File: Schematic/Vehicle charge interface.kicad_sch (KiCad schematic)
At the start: 20 parts

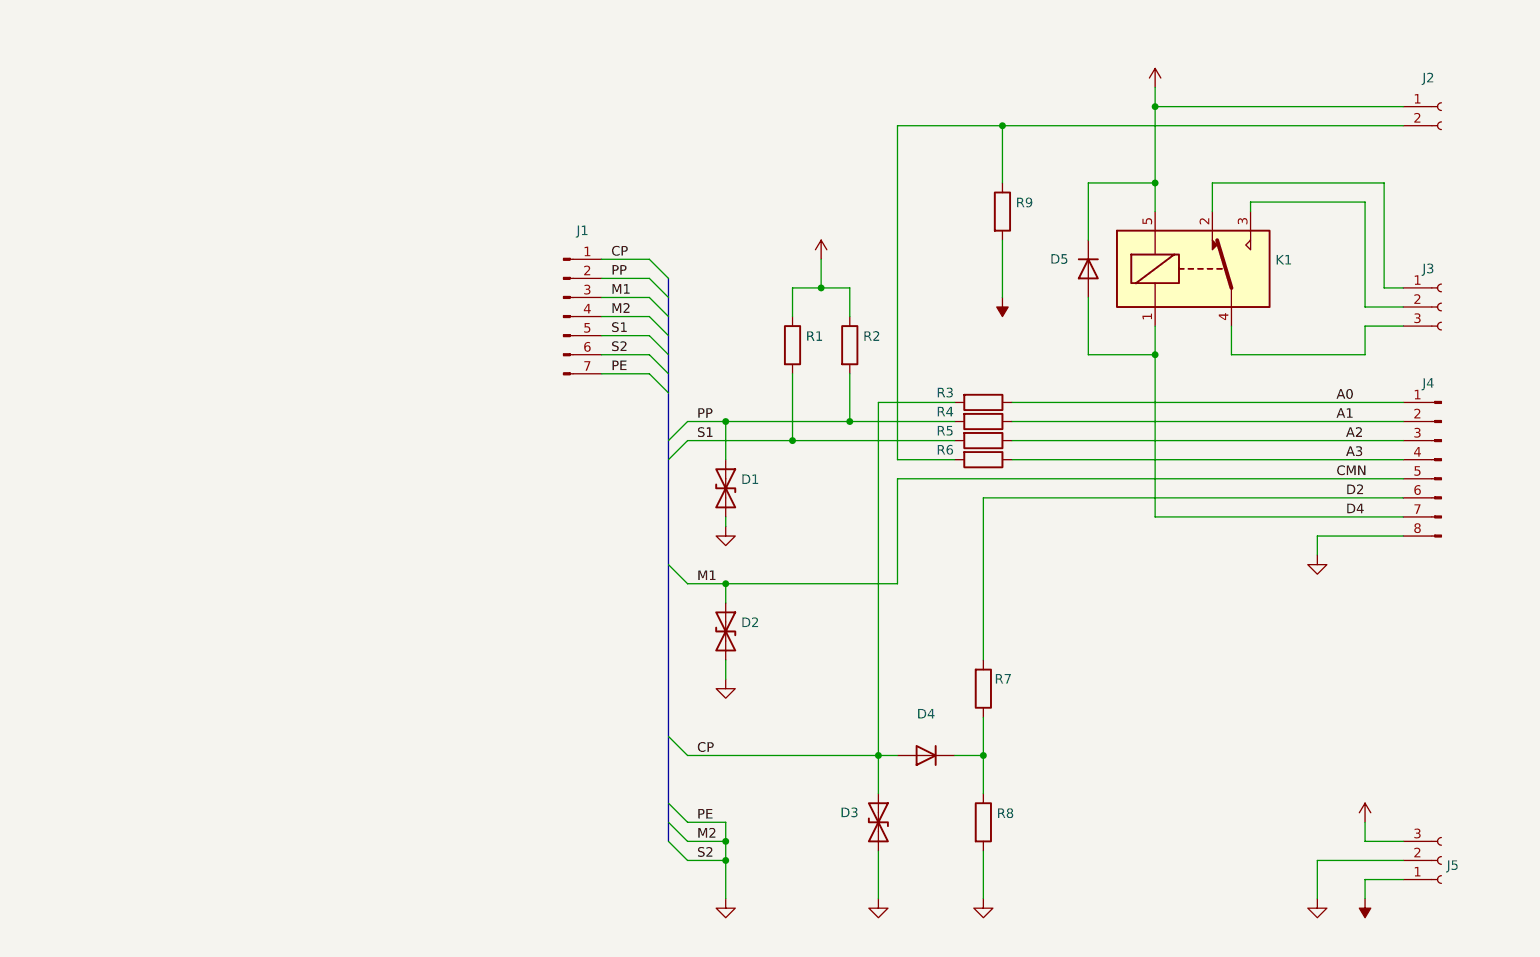
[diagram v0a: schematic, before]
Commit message: Added separate wiring diagram
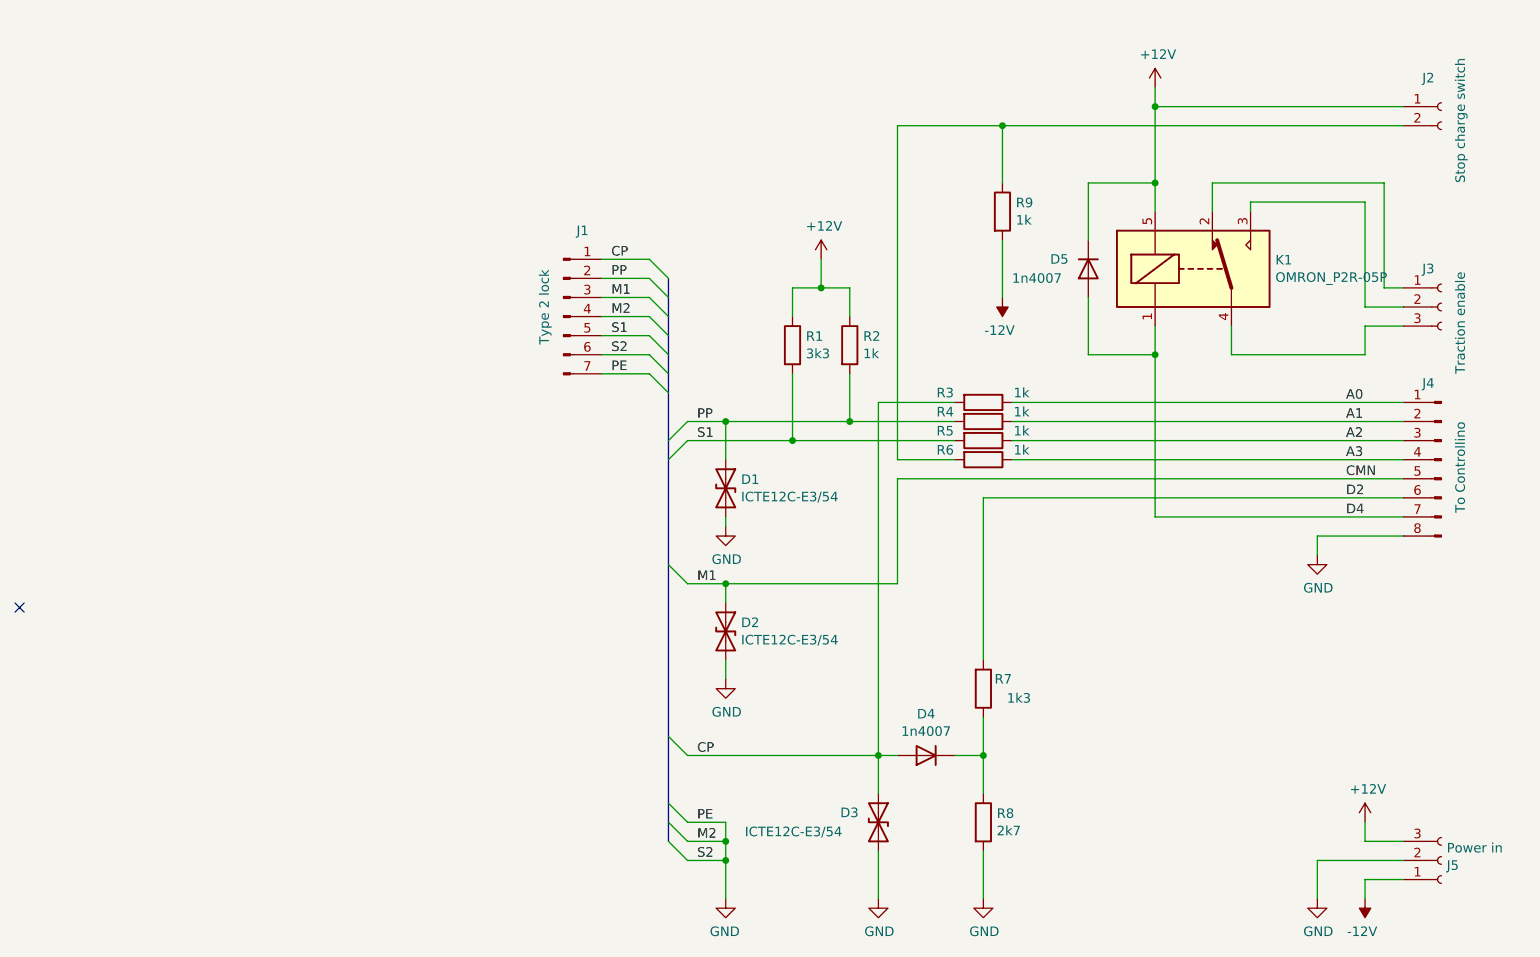
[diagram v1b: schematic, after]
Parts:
- D1, D2, D3: value (none) -> ICTE12C-E3/54; footprint (none) -> Diode_THT:D_DO-201_P15.24mm_Horizontal
- D4, D5: value (none) -> 1n4007; footprint (none) -> Diode_THT:D_DO-41_SOD81_P10.16mm_Horizontal
- J1: value (none) -> Type 2 lock; footprint (none) -> Connector_Wago:Wago_734-137_1x07_P3.50mm_Vertical
- J2: value (none) -> Stop charge switch; footprint (none) -> Connector_Wago:Wago_734-132_1x02_P3.50mm_Vertical
- J3: value (none) -> Traction enable; footprint (none) -> Connector_Wago:Wago_734-133_1x03_P3.50mm_Vertical
- J4: value (none) -> To Controllino; footprint (none) -> Connector_Wago:Wago_734-138_1x08_P3.50mm_Vertical
- J5: value (none) -> Power in; footprint (none) -> Connector_Wago:Wago_734-133_1x03_P3.50mm_Vertical
- K1: value (none) -> OMRON_P2R-05P; footprint (none) -> Downloaded_parts:P2R-05P
- R1: value (none) -> 3k3; footprint (none) -> Resistor_THT:R_Axial_DIN0207_L6.3mm_D2.5mm_P10.16mm_Horizontal
- R2, R3, R4, R5, R6, R9: value (none) -> 1k; footprint (none) -> Resistor_THT:R_Axial_DIN0207_L6.3mm_D2.5mm_P10.16mm_Horizontal
- R7: value (none) -> 1k3; footprint (none) -> Resistor_THT:R_Axial_DIN0207_L6.3mm_D2.5mm_P10.16mm_Horizontal
- R8: value (none) -> 2k7; footprint (none) -> Resistor_THT:R_Axial_DIN0207_L6.3mm_D2.5mm_P10.16mm_Horizontal
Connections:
- no-connect marks 0 -> 1
